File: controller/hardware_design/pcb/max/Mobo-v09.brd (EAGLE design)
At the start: 259.7 x 156.2 mm, 165 parts, among them IC1 TL072, IC10 74HC595N, IC11 74HC595N, IC2 MCP1700, IC3 4050N, IC4 74HC138N, IC5 7908, IC6 2940T-8.0, IC7 7805, IC8 ATMEGA644p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

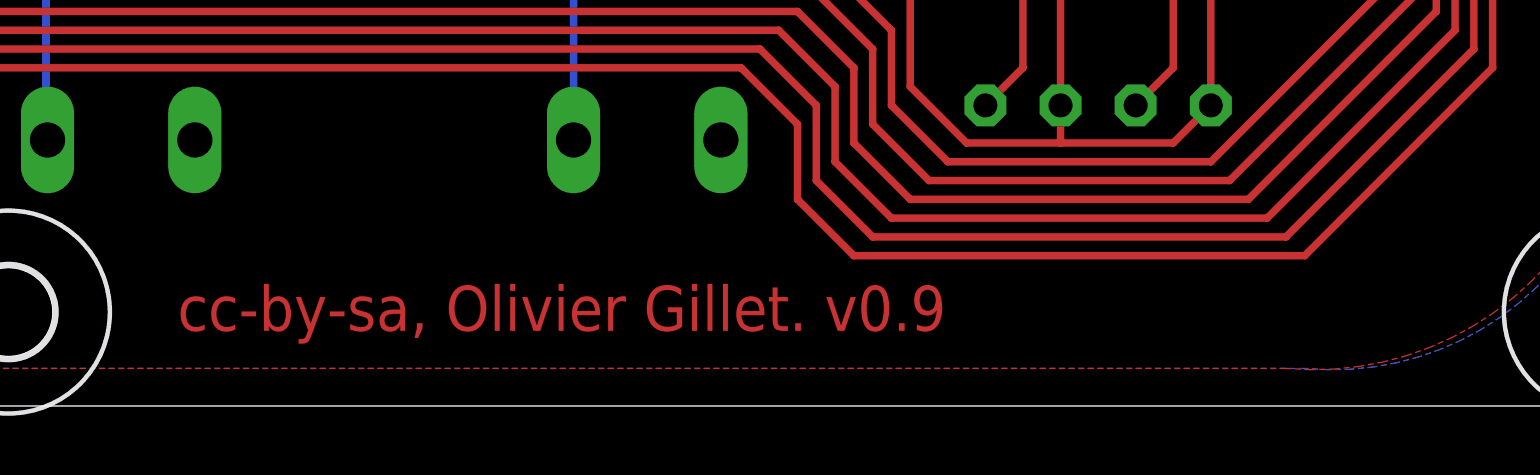
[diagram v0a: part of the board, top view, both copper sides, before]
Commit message: refactoring of variable names and computations, still can't find the final bug...
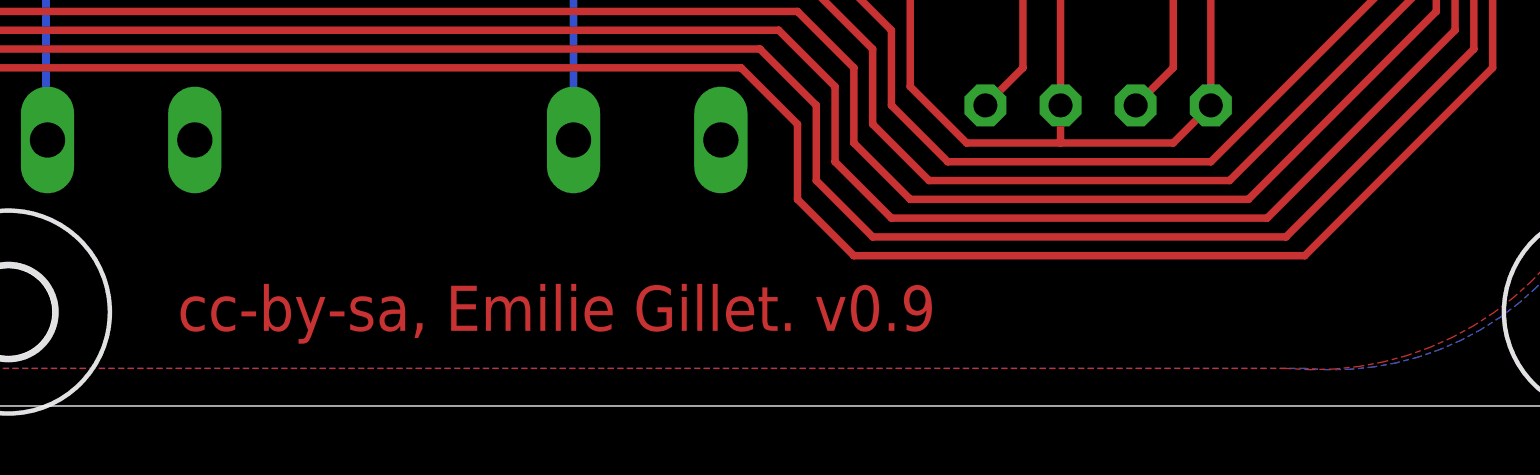
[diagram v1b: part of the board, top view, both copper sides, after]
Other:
- board text added: "cc-by-sa, Emilie Gillet. v0.9"
- board text removed: "cc-by-sa, Olivier Gillet. v0.9"
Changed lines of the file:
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@@
 <text x="223.52" y="121.285" size="1.3208" layer="25" ratio="14">Port 5-6</text>
 <text x="250.825" y="147.32" size="1.9304" layer="26" ratio="15" rot="MR90">9VAC 1A</text>
-<text x="189.865" y="6.35" size="1.524" layer="29" ratio="15">cc-by-sa, Olivier Gillet. v0.9</text>
+<text x="189.865" y="6.35" size="1.524" layer="29" ratio="15">cc-by-sa, Emilie Gillet. v0.9</text>
 <text x="124.46" y="6.35" size="2.54" layer="29" ratio="15">Ambika motherboard</text>
 <text x="124.46" y="6.35" size="2.54" layer="1" ratio="15">Ambika motherboard</text>
-<text x="189.865" y="6.35" size="1.524" layer="1" ratio="15">cc-by-sa, Olivier Gillet. v0.9</text>
+<text x="189.865" y="6.35" size="1.524" layer="1" ratio="15">cc-by-sa, Emilie Gillet. v0.9</text>
 <text x="126.6825" y="129.8575" size="0.8128" layer="25" ratio="14">4.7k to 10K</text>
 <polygon width="0.4064" layer="21" pour="hatch">
